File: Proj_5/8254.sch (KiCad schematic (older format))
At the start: 1 part

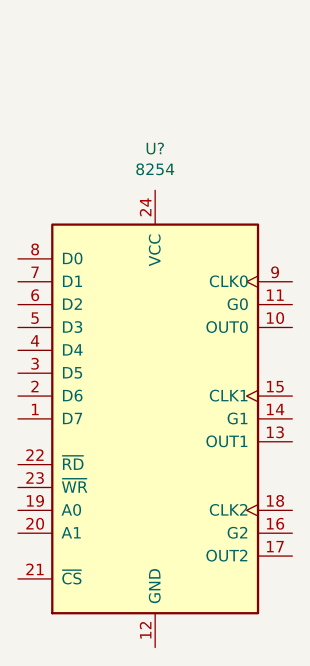
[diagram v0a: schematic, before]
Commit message: Added address decoding
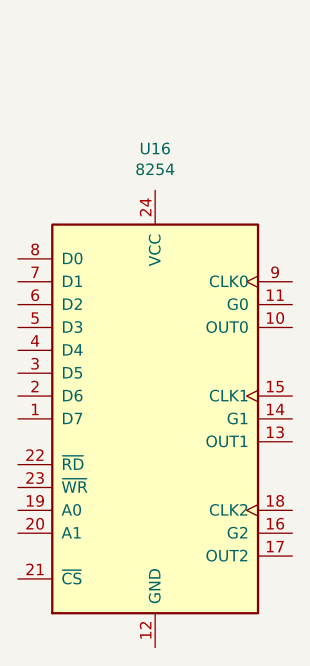
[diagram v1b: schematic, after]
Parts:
- gave numbers to parts that had none: 1
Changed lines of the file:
@@
 $EndDescr
 $Comp
-L Timer:8254 U?
+L Timer:8254 U16
 U 1 1 5EA9C227
 P 5350 3250
-F 0 "U?" H 5350 4431 50  0000 C CNN
+F 0 "U16" H 5350 4431 50  0000 C CNN
 F 1 "8254" H 5350 4340 50  0000 C CNN
 F 2 "Package_DIP:DIP-24_W15.24mm" H 5400 3500 50  0001 C CNN

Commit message: Added Caps to Each Vcc per desc.
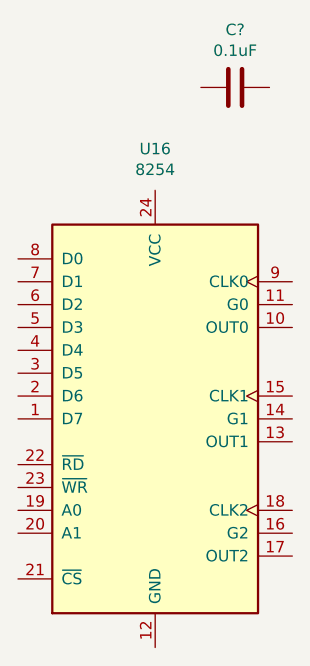
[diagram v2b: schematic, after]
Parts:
- added C?: 0.1uF, symbol Device:C
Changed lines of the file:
@@
 $Descr A4 11693 8268
 encoding utf-8
-Sheet 8 11
+Sheet 7 11
 Title ""
 Date ""
@@
 	1    0    0    -1
 $EndComp
+$Comp
+L Device:C C?
+U 1 1 5EA6A294
+P 5700 1800
+AR Path="/5EA98353/5EA6A294" Ref="C?"  Part="1"
+AR Path="/5EA99146/5EA6A294" Ref="C?"  Part="1"
+F 0 "C?" V 5448 1800 50  0000 C CNN
+F 1 "0.1uF" V 5539 1800 50  0000 C CNN
+F 2 "" H 5738 1650 50  0001 C CNN
+F 3 "~" H 5700 1800 50  0001 C CNN
+	1    5700 1800
+	0    1    1    0
+$EndComp
 $EndSCHEMATC
